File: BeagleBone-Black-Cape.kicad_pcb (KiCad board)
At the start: 2 copper layers, 54.6 x 86.4 mm, 48 parts, among them J1 MC000052, J10 MOLEX_2031, J11 MOLEX_2021, J12 EBV-02-D, J2 MOLEX_2051, J3 MOLEX_2031, J4 MOLEX_2021, J5 MOLEX_2041, J6 MOLEX_2031, J7 MOLEX_2041, J8 MOLEX_2031, J9 MOLEX_2041, P1 BeagleBone_Black_Header, P2 BeagleBone_Black_Header, Q1 IRLB8721PBF, Q2 IRFML8244, U1 DIGIPOT_50K, U2 U_IC-HKB, U3 X_STEPPER, U4 Y_STEPPER, U5 Z_STEPPER

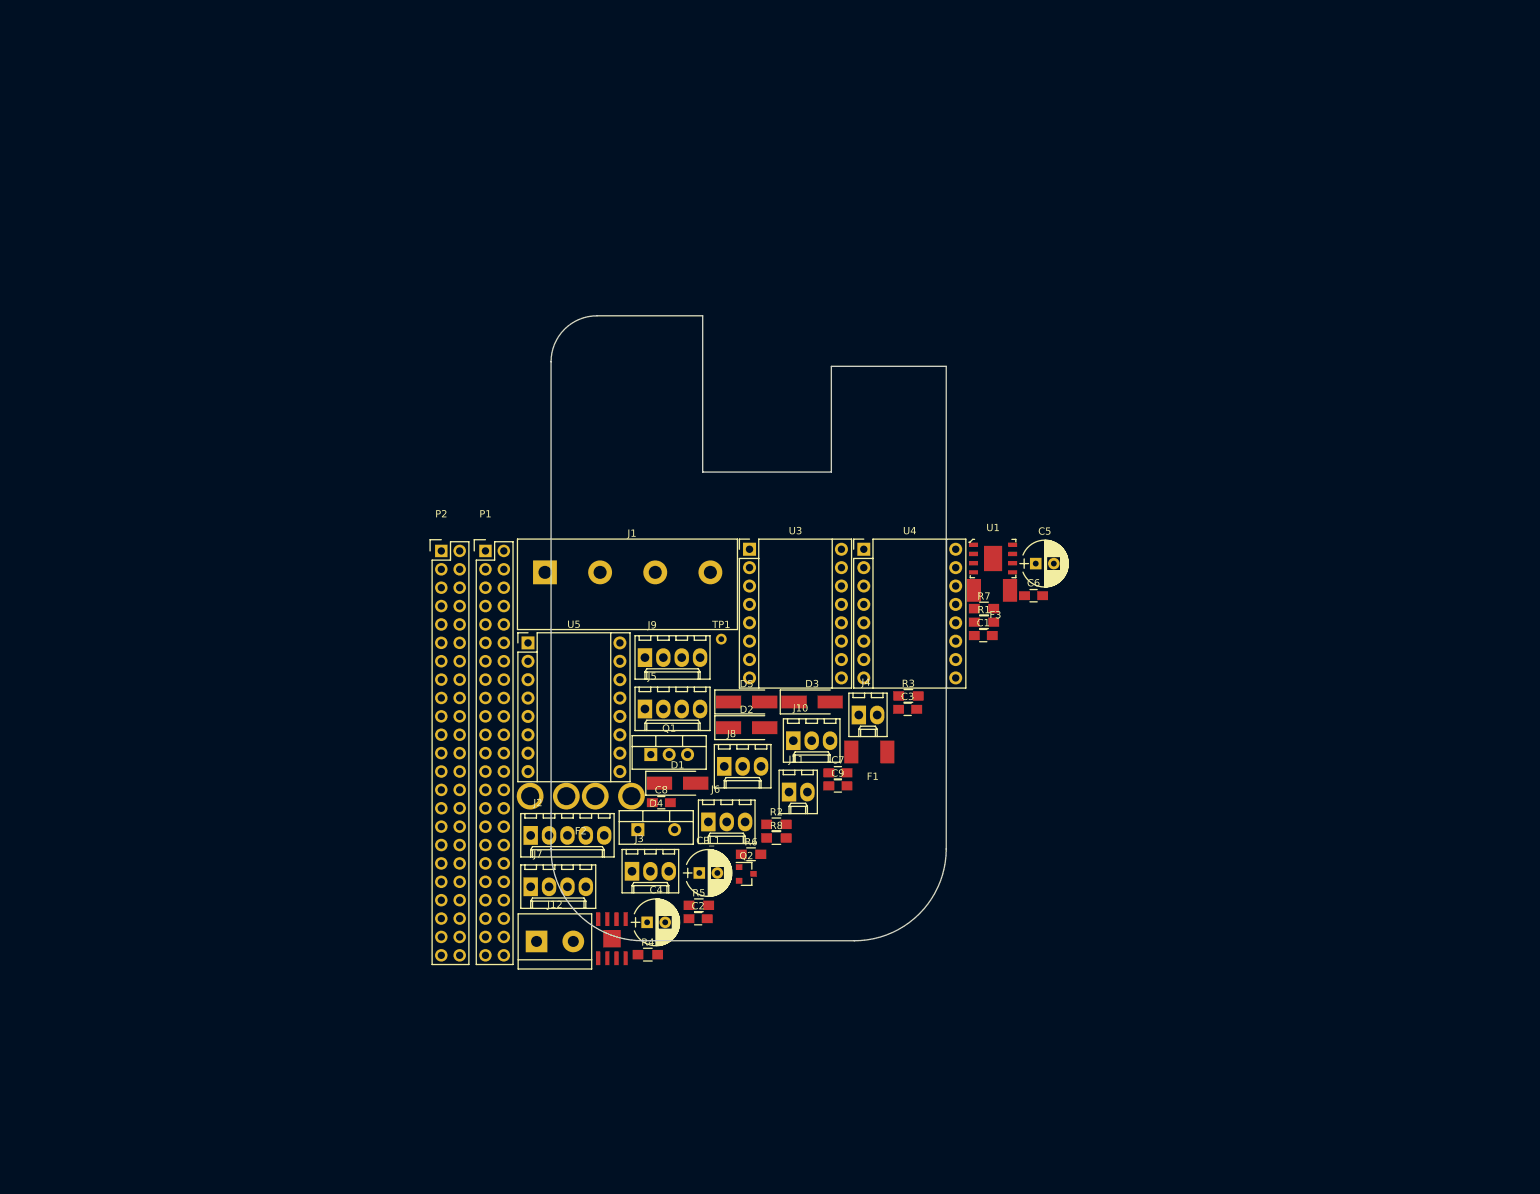
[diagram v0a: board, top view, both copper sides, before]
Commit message: improved organization components cape
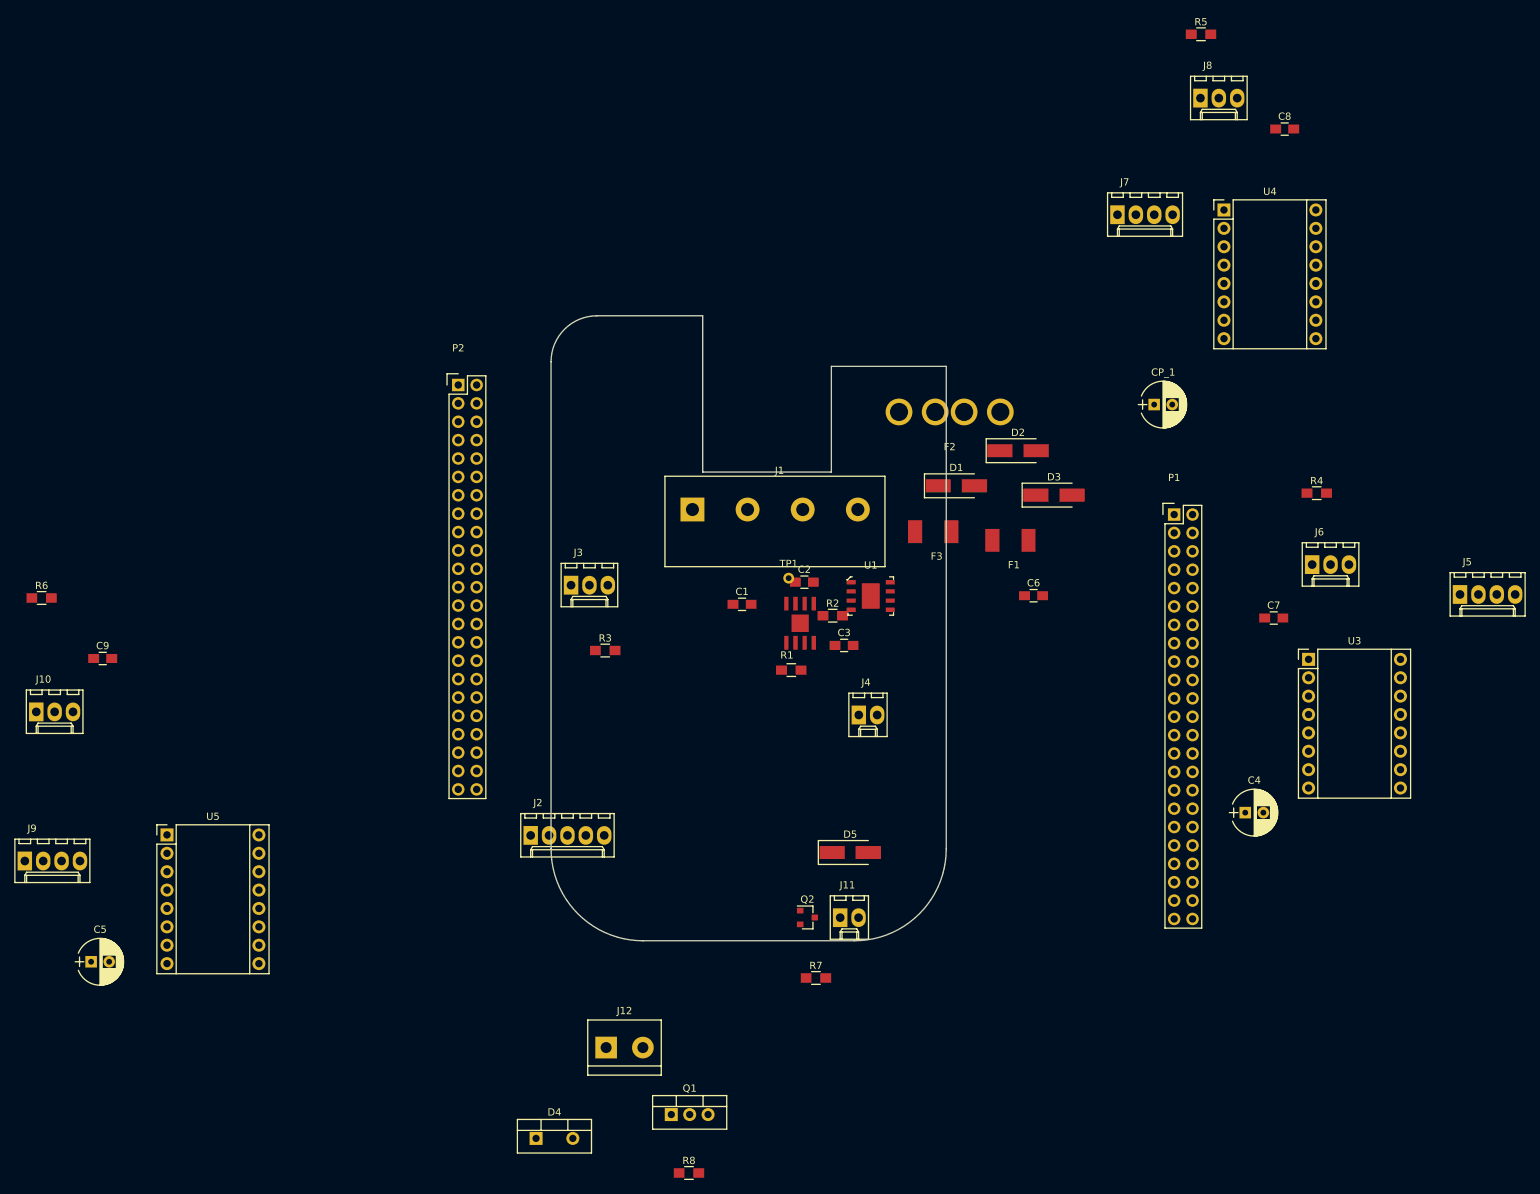
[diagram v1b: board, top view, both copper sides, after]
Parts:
- moved C5 141.7 mm to (50.9, 132.0)
- moved R5 138.9 mm to (204.3, 3.79)
- moved C8 126.8 mm to (215.8, 16.9)
- moved J7 123.3 mm to (192.7, 28.7)
- moved J5 113.7 mm to (240.1, 81.2)
- moved J8 113.4 mm to (204.2, 12.6)
- moved R4 112.3 mm to (220.3, 67.2)
- moved J10 104.7 mm to (43.3, 97.4)
- moved R6 104.2 mm to (44.1, 81.7)
- moved C9 103.1 mm to (52.5, 90.1)
- moved P1 95.3 mm to (200.6, 70.2)
- moved J6 90.7 mm to (219.6, 77.1)
- moved CP_1 90.2 mm to (197.8, 55.0)
- moved J9 90.2 mm to (41.7, 118.0)
- moved C4 84.0 mm to (210.4, 111.4)
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
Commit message: started organizing components for PCB layout
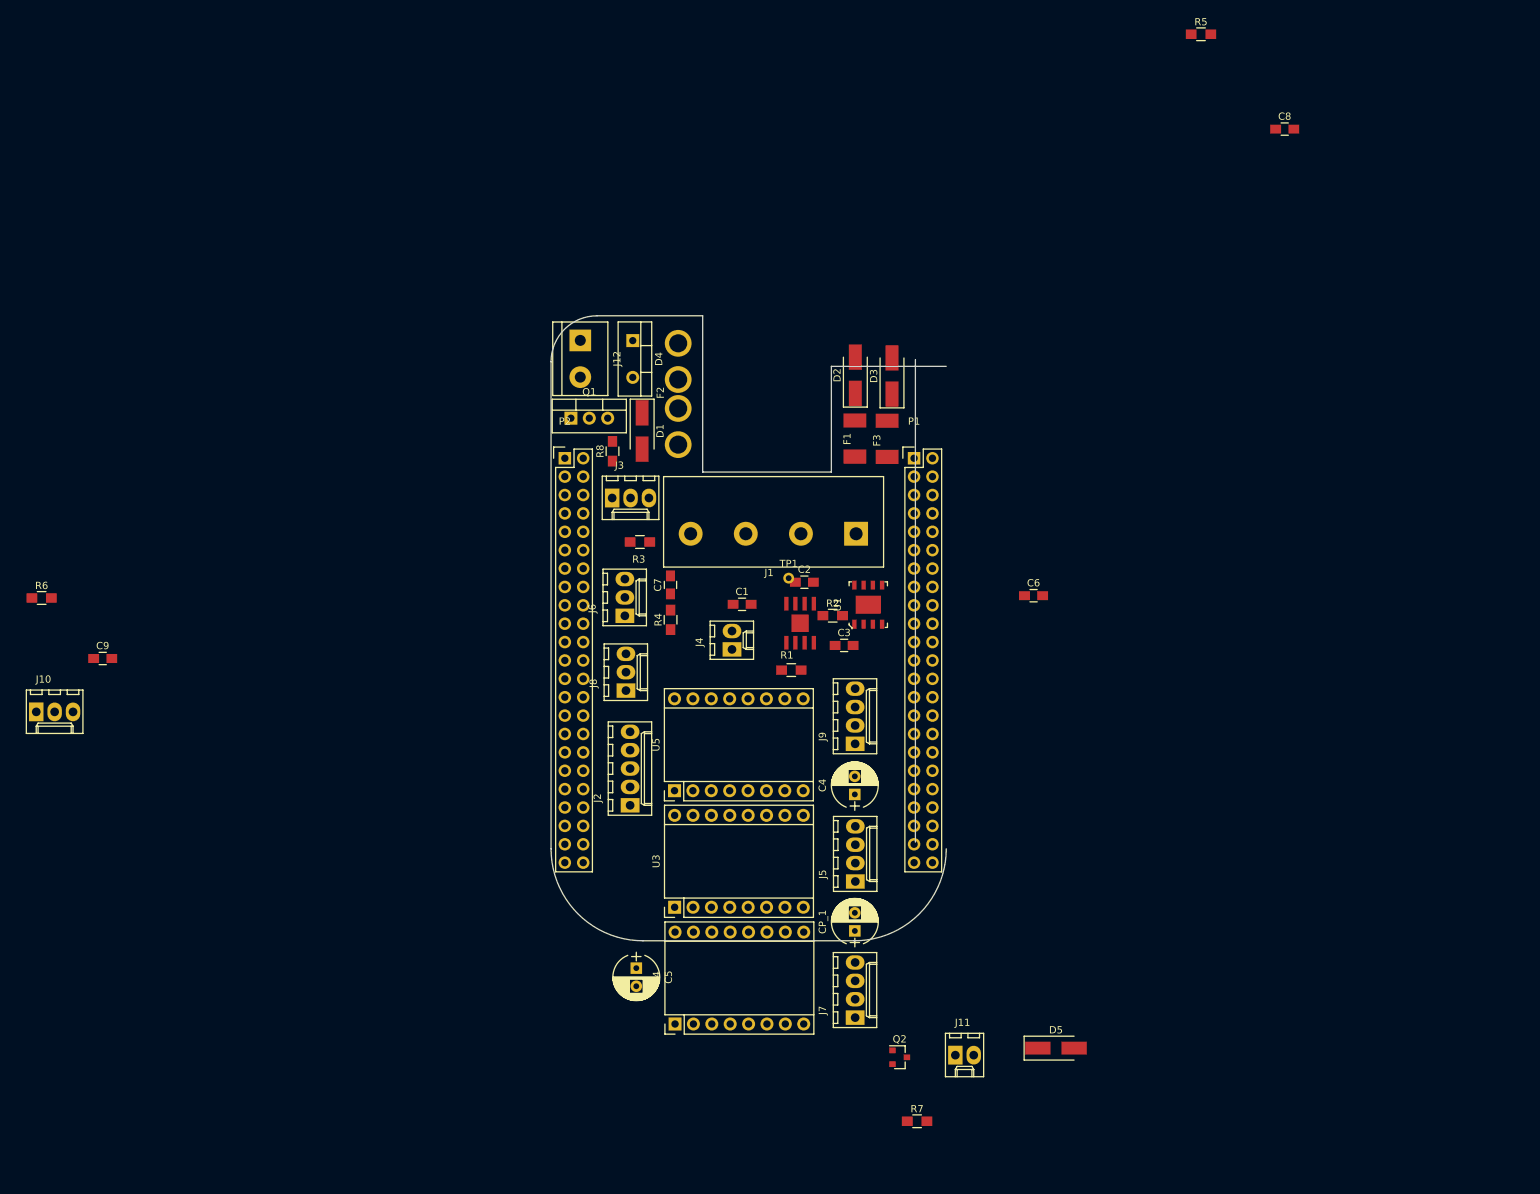
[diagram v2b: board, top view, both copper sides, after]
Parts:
- moved U4 135.7 mm to (131.6, 140.6), turned to 90 degrees
- moved J7 116.7 mm to (156.5, 139.7), turned to 90 degrees
- moved J9 115.9 mm to (156.5, 101.8), turned to 90 degrees
- moved J8 114.0 mm to (124.8, 94.5), turned to 90 degrees
- moved D4 111.0 mm to (125.8, 46.1), turned to 270 degrees
- moved R8 100.3 mm to (123.0, 61.4), turned to 90 degrees
- moved J12 97.8 mm to (118.5, 46.1), turned to 270 degrees
- moved Q1 97.2 mm to (117.2, 56.8)
- moved J6 95.2 mm to (124.7, 84.2), turned to 90 degrees
- moved U3 94.1 mm to (131.5, 124.4), turned to 90 degrees
- moved J5 92.5 mm to (156.5, 120.9), turned to 90 degrees
- moved R4 91.0 mm to (131.0, 84.7), turned to 90 degrees
- moved CP_1 83.7 mm to (156.4, 127.7), turned to 90 degrees
- moved C7 83.5 mm to (131.0, 79.9), turned to 90 degrees
- moved C5 75.3 mm to (126.2, 132.8), turned to 270 degrees
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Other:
- outline, holes or cut-outs redrawn

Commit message: fixed relative imports, started reorganizing pcb
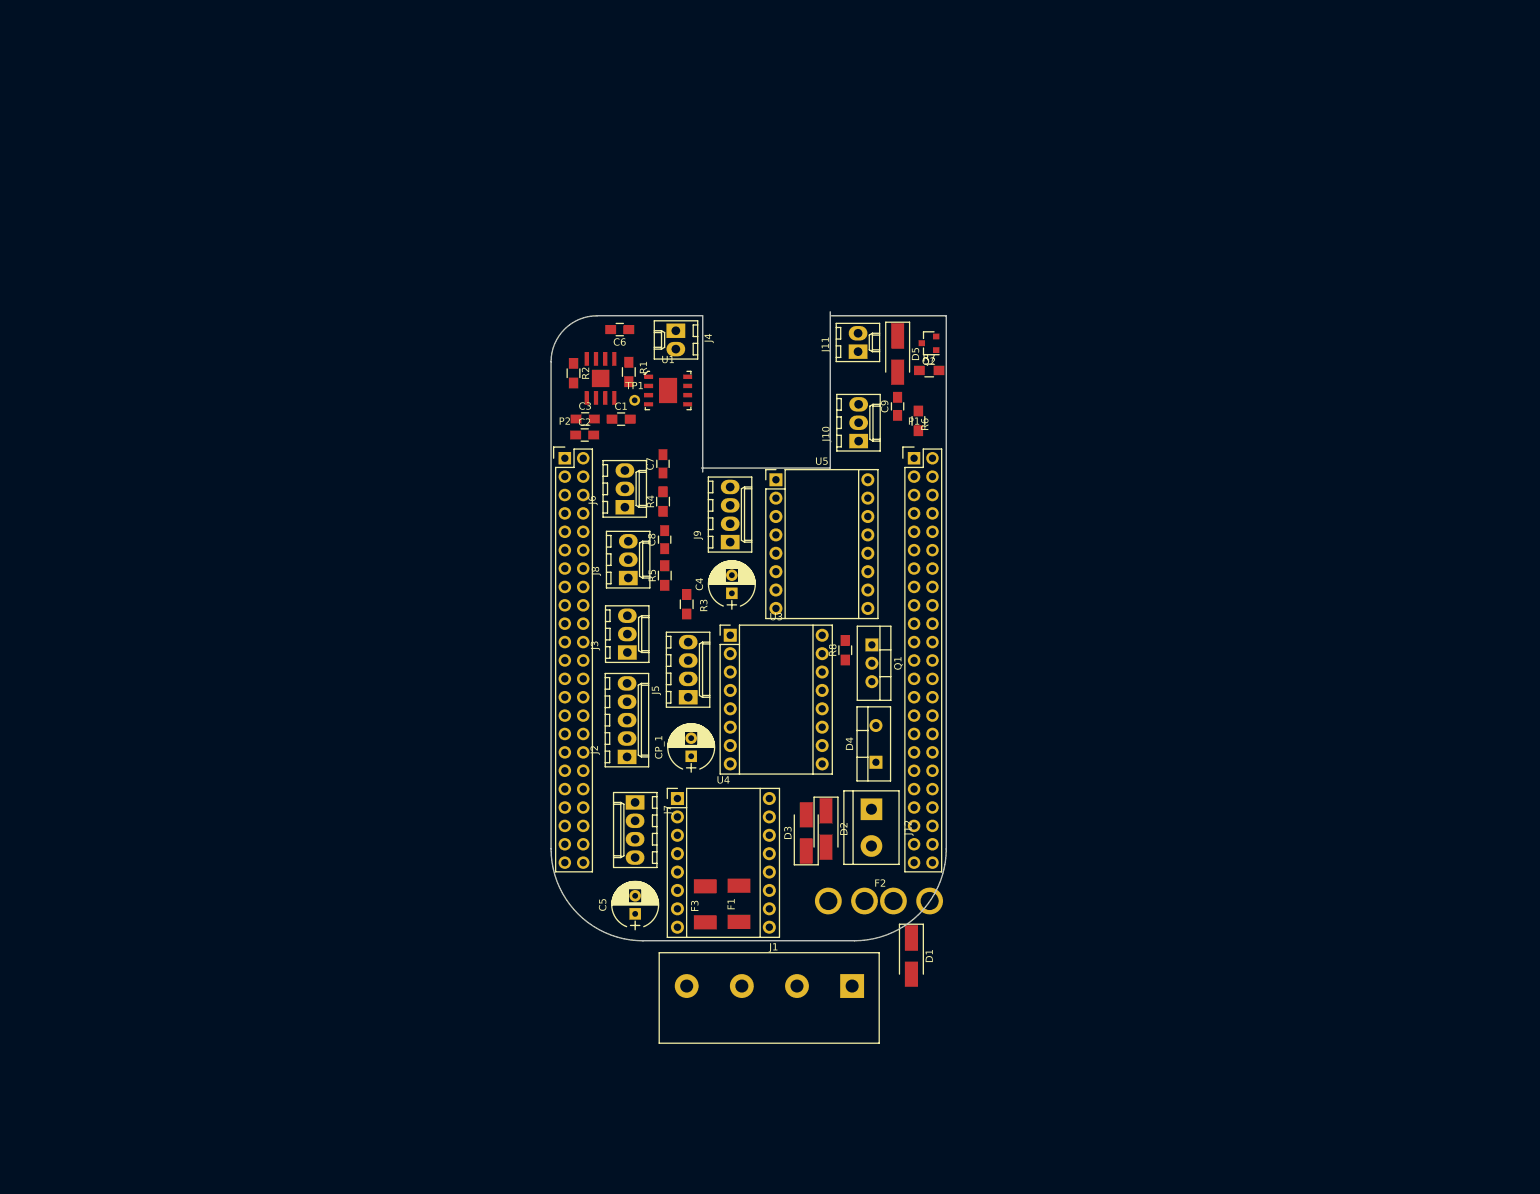
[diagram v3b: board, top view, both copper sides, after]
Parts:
- moved R6 123.6 mm to (165.2, 57.2), turned to 90 degrees
- moved J10 119.6 mm to (157.0, 60.0), turned to 90 degrees
- moved C9 115.2 mm to (162.4, 55.2), turned to 90 degrees
- moved R5 105.3 mm to (130.2, 78.6), turned to 90 degrees
- moved R7 103.8 mm to (166.7, 50.3)
- moved C8 102.8 mm to (130.2, 73.6), turned to 90 degrees
- moved Q2 98.7 mm to (166.7, 46.5), turned to 180 degrees
- moved D5 98.4 mm to (162.4, 48.0), turned to 270 degrees
- moved J11 98.1 mm to (156.9, 47.7), turned to 90 degrees
- moved D1 81.5 mm to (164.3, 131.2)
- moved J12 76.3 mm to (158.7, 110.9)
- moved F2 75.4 mm to (159.8, 123.6), turned to 0 degrees
- moved F3 69.1 mm to (135.8, 124.1)
- moved C6 68.0 mm to (124.0, 44.6), turned to 180 degrees
- moved D4 67.3 mm to (159.4, 104.4), turned to 90 degrees
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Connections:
- U3 pad 1: X_DIR -> X_ENABLE
- U3 pad 2: X_STEP -> SPIO_DI
- U3 pad 3: Net-(U3-Pad3) -> SPIO_SCL
- U3 pad 4: SPIO_DO -> SPI0_CSX
- U3 pad 5: SPI0_CSX -> SPIO_DO
- U3 pad 6: SPIO_SCL -> Net-(U3-Pad6)
- U3 pad 7: SPIO_DI -> X_STEP
- U3 pad 8: X_ENABLE -> X_DIR
- U4 pad 1: Y_DIR -> Y_ENABLE
- U4 pad 2: Y_STEP -> SPIO_DI
- U4 pad 3: Net-(U4-Pad3) -> SPIO_SCL
- U4 pad 4: SPIO_DO -> SPIO_CSY
- U4 pad 5: SPIO_CSY -> SPIO_DO
- U4 pad 6: SPIO_SCL -> Net-(U4-Pad6)
- U4 pad 7: SPIO_DI -> Y_STEP
- U4 pad 8: Y_ENABLE -> Y_DIR
- U5 pad 1: Z_DIR -> Z_ENABLE
- U5 pad 2: Z_STEP -> SPIO_DI
- U5 pad 3: Net-(U5-Pad3) -> SPIO_SCL
- U5 pad 4: SPIO_DO -> SPIO_CSZ
- U5 pad 5: SPIO_CSZ -> SPIO_DO
- U5 pad 6: SPIO_SCL -> Net-(U5-Pad6)
- U5 pad 7: SPIO_DI -> Z_STEP
- U5 pad 8: Z_ENABLE -> Z_DIR
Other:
- board size 54.6 x 86.4 mm -> 54.6 x 86.9 mm
